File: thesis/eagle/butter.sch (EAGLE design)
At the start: 4 parts

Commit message: added eagle files for reals now
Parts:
- removed R1, R2, R3: (no value), resistor:R-US_0414/5V
- removed U$1: ADCS7477, butter:ADCS7477
- added U1, U2, U3, U4, U5, U6, U7, U8: ADCS7477, butter:ADCS7477
- added U10, U11, U12, U13, U14, U15, U16, U9: CD4051BPWR, butter:CD4051BPWR
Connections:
- new net !CS1: U1.!CS
- new net !CS2: U2.!CS
- new net !CS3: U3.!CS
- new net !CS4: U4.!CS
- new net !CS5: U5.!CS
- new net !CS6: U6.!CS
- new net !CS7: U7.!CS
- new net !CS8: U8.!CS
- new net D1: U1.SDATA
- new net D2: U2.SDATA
- new net D3: U3.SDATA
- new net D4: U4.SDATA
- new net D5: U5.SDATA
- new net D6: U6.SDATA
- new net D7: U7.SDATA
- new net D8: U8.SDATA
- new net GND: U1.GND, U2.GND, U3.GND, U4.GND, U5.GND, U6.GND, U7.GND, U8.GND
- new net N$6: U14.Z, U6.IN
- new net N$7: U15.Z, U7.IN
- new net N$8: U16.Z, U8.IN
- new net SCK: U1.SCLK, U2.SCLK, U3.SCLK, U4.SCLK, U5.SCLK, U6.SCLK, U7.SCLK, U8.SCLK
- new net VCC: U1.VDD, U2.VDD, U3.VDD, U4.VDD, U5.VDD, U6.VDD, U7.VDD, U8.VDD
- net N$1: now also U1.IN, U9.Z; no longer R1.1, U$1.VDD
- net N$2: now also U10.Z, U2.IN; no longer R2.1, U$1.GND
- net N$3: now also U11.Z, U3.IN; no longer R3.2, U$1.IN
- net N$4: now also U12.Z, U4.IN; no longer R1.2, R3.1
- net N$5: now also U13.Z, U5.IN; no longer R2.2, U$1.SDATA

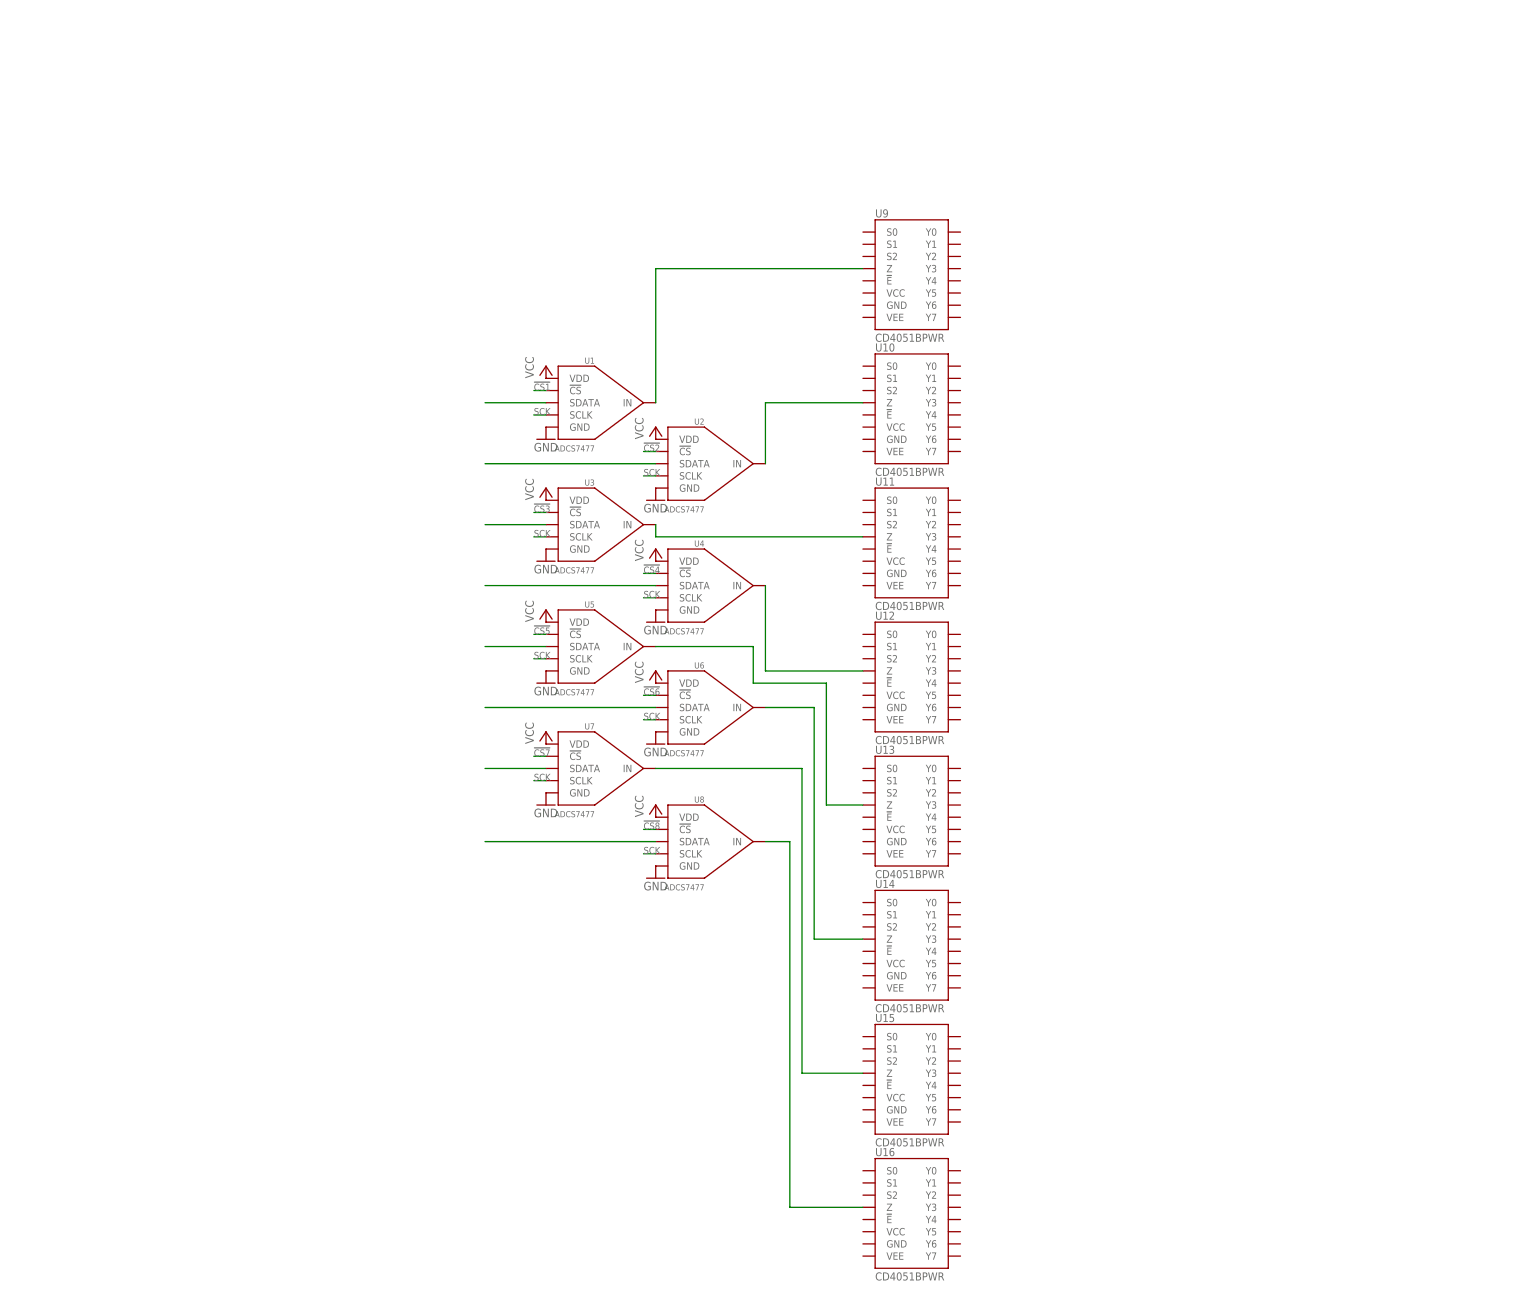
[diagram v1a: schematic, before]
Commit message: added stm32f4 breakout to design, starting with two ADCs and two multiplexers
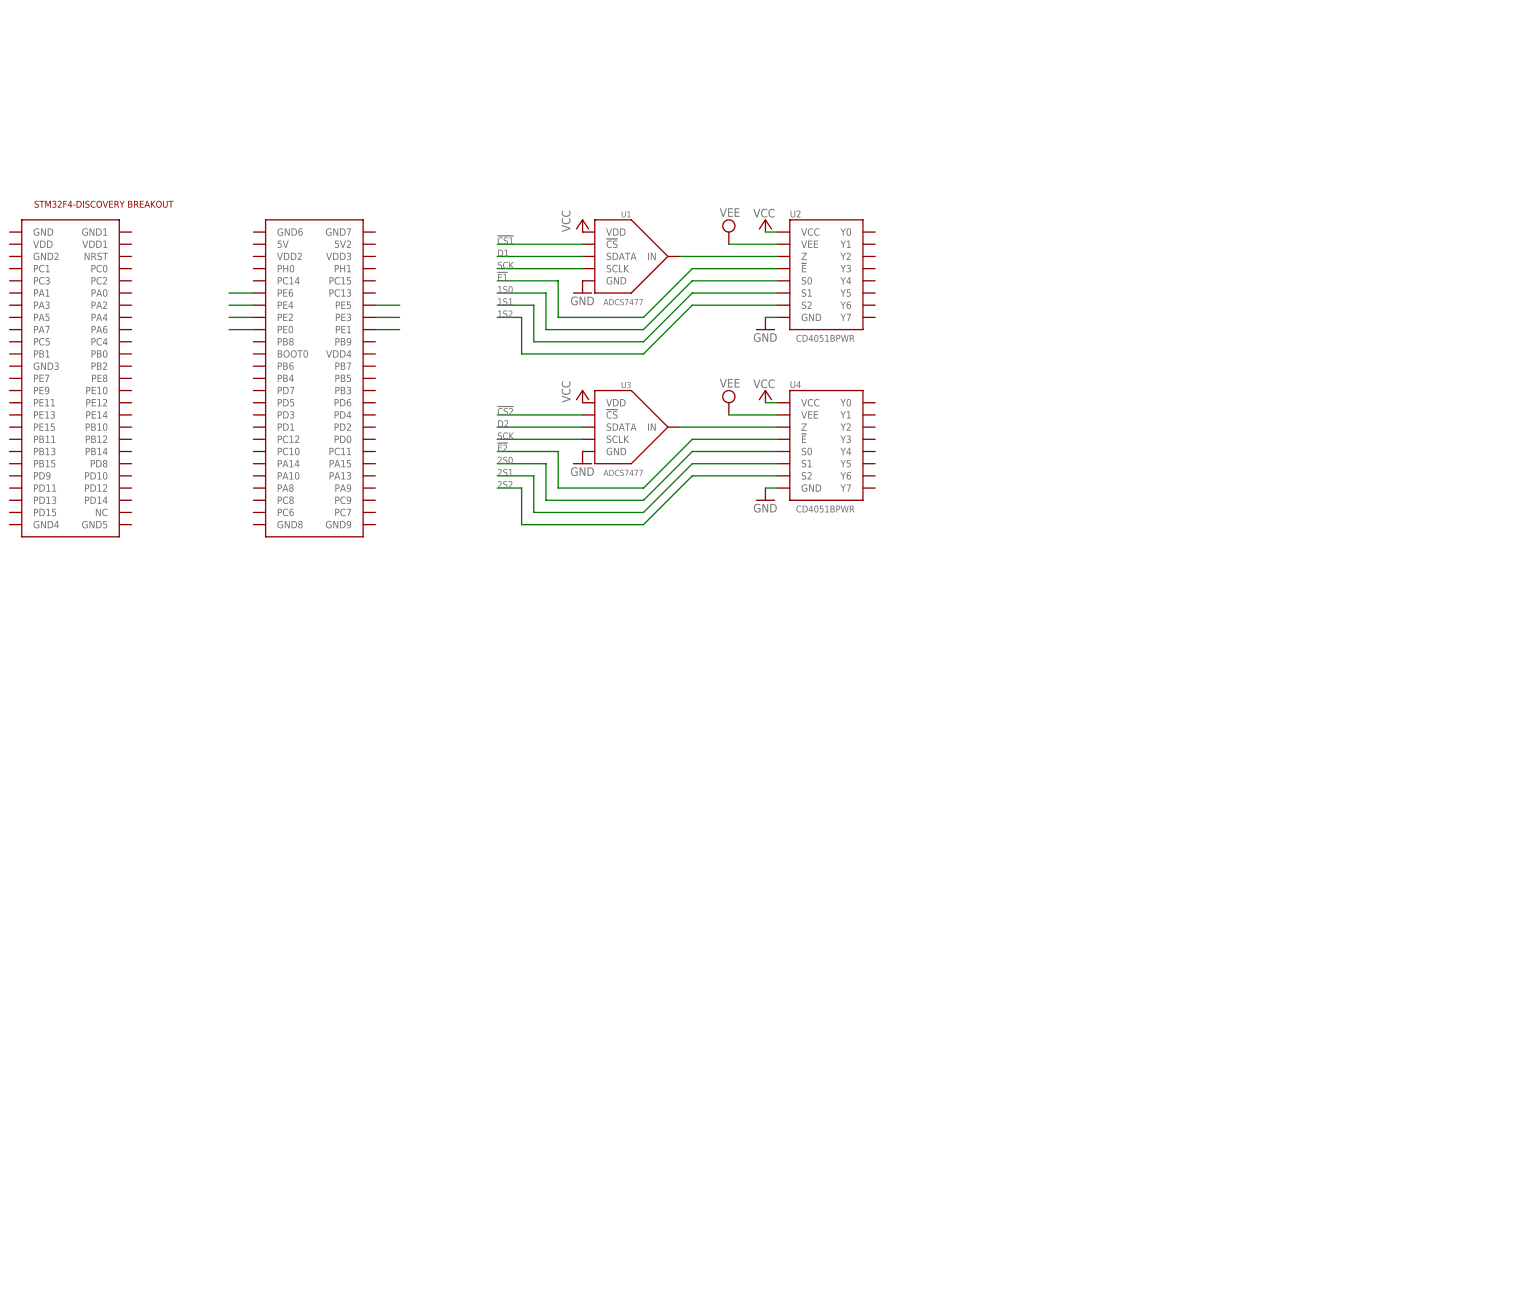
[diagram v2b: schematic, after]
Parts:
- removed U10, U11, U12, U13, U14, U15, U16, U9: CD4051BPWR, butter:CD4051BPWR
- removed U5, U6, U7, U8: ADCS7477, butter:ADCS7477
- added U$1: STM32F4-DISCOVERY, STM32F4-DISCOVERY:STM32F4-DISCOVERY
- U2, U4: value ADCS7477 -> CD4051BPWR; device butter:ADCS7477 -> butter:CD4051BPWR
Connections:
- removed net !CS3: U3.!CS
- removed net !CS4: U4.!CS
- removed net !CS5: U5.!CS
- removed net !CS6: U6.!CS
- removed net !CS7: U7.!CS
- removed net !CS8: U8.!CS
- removed net D3: U3.SDATA
- removed net D4: U4.SDATA
- removed net D5: U5.SDATA
- removed net D6: U6.SDATA
- removed net D7: U7.SDATA
- removed net D8: U8.SDATA
- removed net N$3: U11.Z, U3.IN
- removed net N$4: U12.Z, U4.IN
- removed net N$5: U13.Z, U5.IN
- removed net N$6: U14.Z, U6.IN
- removed net N$7: U15.Z, U7.IN
- removed net N$8: U16.Z, U8.IN
- new net !E1: U$1.PE3, U2.!E
- new net !E2: U4.!E
- new net 1S0: U$1.PE4, U2.S0
- new net 1S1: U$1.PE5, U2.S1
- new net 1S2: U$1.PE6, U2.S2
- new net 2S0: U4.S0
- new net 2S1: U4.S1
- new net 2S2: U4.S2
- new net VEE: U2.VEE, U4.VEE
- net !CS1: now also U$1.PE2
- net !CS2: now also U3.!CS; no longer U2.!CS
- net D1: now also U$1.PE1
- net D2: now also U3.SDATA; no longer U2.SDATA
- net GND: no longer U5.GND, U6.GND, U7.GND, U8.GND
- net N$1: now also U2.Z; no longer U9.Z
- net N$2: now also U3.IN, U4.Z; no longer U10.Z, U2.IN
- net SCK: now also U$1.PE0; no longer U2.SCLK, U4.SCLK, U5.SCLK, U6.SCLK, U7.SCLK, U8.SCLK
- net VCC: now also U2.VCC, U4.VCC; no longer U2.VDD, U4.VDD, U5.VDD, U6.VDD, U7.VDD, U8.VDD
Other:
- moved on the sheet: U1, U3

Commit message: started designing rail interface
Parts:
- added IC1: TL072D, linear:TL072D
- added JP1: (no value), pinhead:PINHD-1X1
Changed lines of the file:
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@@
 <part name="SUPPLY2" library="supply2" deviceset="VEE" device=""/>
 <part name="U$1" library="STM32F4-DISCOVERY" deviceset="STM32F4-DISCOVERY" device=""/>
+<part name="IC1" library="linear" deviceset="TL072" device="D"/>
+<part name="JP1" library="pinhead" deviceset="PINHD-1X1" device=""/>
 </parts>
 <sheets>
@@
 <instance part="SUPPLY2" gate="G$1" x="63.5" y="50.8"/>
 <instance part="U$1" gate="G$1" x="-48.26" y="58.42"/>
+<instance part="IC1" gate="A" x="119.38" y="99.06"/>
+<instance part="IC1" gate="B" x="119.38" y="114.3" rot="R180"/>
+<instance part="JP1" gate="G$1" x="170.18" y="101.6"/>
 </instances>
 <busses>

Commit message: whatever, fuck it
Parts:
- removed JP1: (no value), pinhead:PINHD-1X1
- removed U3: ADCS7477, butter:ADCS7477
- removed U4: CD4051BPWR, butter:CD4051BPWR
- added R1, R2, R3: (no value), resistor:R-US_R0603
- added U$10, U$11, U$12, U$13, U$2, U$7, U$8, U$9: DG467, butter:DG467
- added U$3, U$4, U$5, U$6: RAILSEP, butter:RAILSEP
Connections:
- removed net !CS2: U3.!CS
- removed net !E2: U4.!E
- removed net 2S0: U4.S0
- removed net 2S1: U4.S1
- removed net 2S2: U4.S2
- removed net D2: U3.SDATA
- new net N$10: U$11G$1.COM, U$5.R, U2.Y5
- new net N$11: U$12G$1.COM, U$6.L, U2.Y6
- new net N$12: U$13G$1.COM, U$6.R, U2.Y7
- new net N$13: U$2G$1.CTL
- new net N$14: U$8G$1.CTL
- new net N$15: U$10G$1.CTL
- new net N$16: U$12G$1.CTL
- new net N$17: U$7G$1.CTL
- new net N$18: U$9G$1.CTL
- new net N$19: U$11G$1.CTL
- new net N$20: U$13G$1.CTL
- new net N$21: U$10G$1.IN, U$11G$1.IN, U$12G$1.IN, U$13G$1.IN, U$2G$1.IN, U$7G$1.IN, U$8G$1.IN, U$9G$1.IN
- new net N$3: U$2G$1.COM, U$3.L, U2.Y0
- new net N$4: IC1B.+IN, U2.Z
- new net N$5: IC1A.-IN, R1.1, R2.2, R3.2
- new net N$6: IC1B.-IN, IC1B.OUT, R1.2
- new net N$7: U$4.L, U$8G$1.COM, U2.Y2
- new net N$8: U$4.R, U$9G$1.COM, U2.Y3
- new net N$9: U$10G$1.COM, U$5.L, U2.Y4
- net GND: now also IC1A.+IN, U$10G$2.GND, U$11G$2.GND, U$12G$2.GND, U$13G$2.GND, U$2G$2.GND, U$7G$2.GND, U$8G$2.GND, U$9G$2.GND; no longer U3.GND, U4.GND
- net N$1: now also IC1A.OUT, R2.1; no longer U2.Z
- net N$2: now also U$3.R, U$7G$1.COM, U2.Y1; no longer U3.IN, U4.Z
- net SCK: no longer U3.SCLK
- net VCC: now also IC1P.V+, U$10G$2.VCC, U$11G$2.VCC, U$12G$2.VCC, U$13G$2.VCC, U$2G$2.VCC, U$7G$2.VCC, U$8G$2.VCC, U$9G$2.VCC; no longer U3.VDD, U4.VCC
- net VEE: now also IC1P.V-, U$10G$2.VEE, U$11G$2.VEE, U$12G$2.VEE, U$13G$2.VEE, U$2G$2.VEE, U$7G$2.VEE, U$8G$2.VEE, U$9G$2.VEE; no longer U4.VEE
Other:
- moved on the sheet: IC1A, IC1B, U1, U2

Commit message: rev 1a!
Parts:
- added C1, C3, C6: .1u, rcl:C-EUC0805
- added C2, C4, C7: 1u, rcl:C-EUC0805
- added C5: (no value), rcl:C-EUC0805
- added JMP1, JMP2, JMP3, JMP4: (no value), butter:JMP
- added JP1: (no value), pinhead:PINHD-1X3
- added R4, R5, R6, R7: (no value), resistor:R-US_R0603
- added U3: (no value), butter:MCP6S93
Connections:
- new net !CSP1: U$1.PB8, U3.!CS
- new net +5V: C1.1, C2.1, C3.1, C4.1, C6.1, C7.1, R4.2, U$1.5V, U1.VDD, U3.VDD
- new net N$22: IC1A.+IN, JMP3.P$2, R1.1, R2.2, R7.1
- new net N$23: R3.2, R4.1, U3.VREF
- new net N$24: JMP2.P$2, JMP3.P$1, JMP4.P$1, U1.IN
- new net N$25: U3.SO
- new net N$26: IC1A.OUT, JMP4.P$2, R5.1
- new net N$27: R7.2, U3.CH0
- net D1: now also U3.SI
- net GND: now also C1.2, C2.2, C3.2, C4.2, C6.2, C7.2, JP1.2, R3.1, R6.1, U$1.GND8, U3.VSS; no longer IC1A.+IN
- net N$1: now also IC1A.-IN, R5.2, R6.2; no longer IC1A.OUT, R2.1, U1.IN
- net N$10: now also U2.Y2; no longer U2.Y5
- net N$12: now also U2.Y1; no longer U2.Y7
- net N$2: now also U2.Y0; no longer U2.Y1
- net N$3: now also U$4.L, U2.Y5; no longer U$3.L, U2.Y0
- net N$4: now also JMP1.P$2
- net N$5: now also JMP2.P$1, U3.VO; no longer IC1A.-IN, R1.1, R2.2, R3.2
- net N$6: now also JMP1.P$1
- net N$7: now also U$3.L, U2.Y7; no longer U$4.L, U2.Y2
- net SCK: now also U3.SCK
- net VCC: now also JP1.3; no longer U1.VDD
- net VEE: now also JP1.1, R2.1
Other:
- moved on the sheet: IC1A, IC1B, R1, R2, R3, U$10, U$11, U$12, U$13, U$2, U$3, U$4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

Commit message: not sure what's new here, but updated butter board
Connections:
- net +5V: now also C5.1
- net GND: now also C5.2
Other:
- moved on the sheet: C5
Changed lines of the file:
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@@
 <part name="P+13" library="supply1" deviceset="+5V" device=""/>
 <part name="P+14" library="supply1" deviceset="+5V" device=""/>
+<part name="GND14" library="supply1" deviceset="GND" device=""/>
+<part name="P+15" library="supply1" deviceset="+5V" device=""/>
 </parts>
 <sheets>
@@
 <instance part="C3" gate="G$1" x="27.94" y="43.18"/>
 <instance part="C4" gate="G$1" x="35.56" y="43.18"/>
-<instance part="C5" gate="G$1" x="50.8" y="121.92"/>
+<instance part="C5" gate="G$1" x="68.58" y="116.84"/>
 <instance part="C6" gate="G$1" x="127" y="55.88"/>
 <instance part="C7" gate="G$1" x="137.16" y="55.88"/>
@@
 <instance part="P+14" gate="1" x="137.16" y="60.96" smashed="yes">
 <attribute name="VALUE" x="138.938" y="62.738" size="1.778" layer="96" rot="R180"/>
+</instance>
+<instance part="GND14" gate="1" x="68.58" y="109.22"/>
+<instance part="P+15" gate="1" x="68.58" y="121.92" smashed="yes">
+<attribute name="VALUE" x="70.358" y="123.698" size="1.778" layer="96" rot="R180"/>
 </instance>
 </instances>
@@
 <pinref part="C7" gate="G$1" pin="2"/>
 <pinref part="GND13" gate="1" pin="GND"/>
+</segment>
+<segment>
+<pinref part="C5" gate="G$1" pin="2"/>
+<pinref part="GND14" gate="1" pin="GND"/>
 </segment>
 </net>
@@
 <pinref part="P+14" gate="1" pin="+5V"/>
 </segment>
-</net>
+<segment>
+<pinref part="C5" gate="G$1" pin="1"/>
+<pinref part="P+15" gate="1" pin="+5V"/>
+</segment>
+</net>
